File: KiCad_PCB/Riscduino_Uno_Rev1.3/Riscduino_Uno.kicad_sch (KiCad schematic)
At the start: 87 parts, among them J10 Conn_01x06_Pin, J11 USB_B_Micro, J12 Conn_01x08_Pin, J13 Conn_01x10_Pin, J2 Conn_01x03_Pin, J3 Conn_01x01, J4 Conn_02x04_Odd_Even, J5 ISP, J6 Conn_01x01, J7 Conn_01x01, J8 Conn_01x01, J9 Conn_01x08_Pin, SW1 4Pin Round Button SPST Straig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, U2 W25Q32JVSS, U3 23LC1024-I/P, U4 W25Q32JVSS, U5 Riscduino, U6 LM1117MP-3.3, U7 LM1117S-ADJ, U8 CH340C, X1 ASE-10.000MHZ-LC-T

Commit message: Update
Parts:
- added R19, R25: 0E, Riscduino:R_0603_1608Metric_Pad0.98x0.95mm_HandSolder, symbol Device:R
- D1: renamed from D2; footprint Riscduino:LED_0805_2012Metric_Pad1.15x1.40mm_HandSolder -> Riscduino.Library:LED_0805_2012Metric_Pad1.15x1.40mm_HandSolder
- D2: renamed from D3; footprint Riscduino:LED_0805_2012Metric_Pad1.15x1.40mm_HandSolder -> Riscduino.Library:LED_0805_2012Metric_Pad1.15x1.40mm_HandSolder
- D3: renamed from D1; footprint Riscduino:LED_0805_2012Metric_Pad1.15x1.40mm_HandSolder -> Riscduino.Library:LED_0805_2012Metric_Pad1.15x1.40mm_HandSolder
- D4, D5: footprint Riscduino:LED_0805_2012Metric_Pad1.15x1.40mm_HandSolder -> Riscduino.Library:LED_0805_2012Metric_Pad1.15x1.40mm_HandSolder
- X1: footprint Riscduino:Crystal_SMD_Abracon_ABM8G-4Pin_3.2x2.5mm -> Riscduino.Library:Crystal_SMD_Abracon_ABM8G-4Pin_3.2x2.5mm
- renumbered C6 to C10, C8 to C11, C14 to C12, C16 to C13, C19 to C14, C17 to C16, C18 to C17, C22 to C18, C21 to C19, C23 to C20, C24 to C21, C25 to C22, C10 to C23, C12 to C24, C20 to C25, C7 to C5, C9 to C6, C11 to C7, C13 to C8, C5 to C9, J5 to J1, J13 to J10, J2 to J11, J7 to J12, J10 to J2, J9 to J3, J6 to J4, J3 to J5, J4 to J6, J8 to J7, J11 to J8, J12 to J9, JP2 to JP1, JP1 to JP2, R2 to R1, R12 to R10, R5 to R11, R32 to R12, R14 to R13, R19 to R14, R23 to R15, R20 to R16, R21 to R17, R22 to R18, R4 to R2, R25 to R20, R27 to R21, R29 to R22, R28 to R23, R33 to R24, R15 to R26, R16 to R27, R24 to R28, R26 to R29, R6 to R3, R7 to R4, R3 to R5, R9 to R6, R8 to R7, R13 to R8, R11 to R9, U4 to U1, U3 to U2, U5 to U3, U6 to U4, U8 to U5, U7 to U6, U2 to U7
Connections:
- net ardunio_d0: now also R19.2; no longer U5.2 (TXD)
- net ardunio_d1: now also R25.2; no longer U5.3 (RXD)
- net mprj_io_12: no longer J10.8 (Pin_8)
- net mprj_io_30: now also J10.8 (Pin_8)
- new net: R19.1, U5.2 (TXD)
- new net: R25.1, U5.3 (RXD)

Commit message: Power Supervisory Circuit
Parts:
- added C28: 0.1uf, Riscduino.Library:C_0603_1608Metric_Pad1.08x0.95mm_HandSolder, symbol Device:C
- added U8: APX811, Package_TO_SOT_SMD:SOT-143_Handsoldering, symbol Power_Supervisor:MIC811TUY
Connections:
- net +3.3V: now also C28.1, U8.4 (VCC)
- net GND: now also C28.2, U8.1 (GND)
- net ~{RST}: now also U8.2 (~{RESET}); no longer C3.1, R1.2, R12.2, SW1.2
- new net ~{MR}: C3.1, R1.2, R12.2, SW1.2, U8.3 (~{MR})
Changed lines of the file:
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@@
   (junction (at 328.93 37.084) (diameter 0) (color 0 0 0 0)
   )
+  (junction (at 361.95 247.65) (diameter 0) (color 0 0 0 0)
+  )
   (junction (at 80.01 206.248) (diameter 0) (color 0 0 0 0)
   )
@@
   (junction (at 328.168 196.342) (diameter 0) (color 0 0 0 0)
   )
+  (junction (at 326.39 262.89) (diameter 0) (color 0 0 0 0)
+  )
   (junction (at 330.708 173.228) (diameter 0) (color 0 0 0 0)
   )
@@
     (stroke (width 0) (type default))
   )
-  (wire (pts (xy 323.85 262.89) (xy 332.994 262.89))
+  (wire (pts (xy 323.85 262.89) (xy 326.39 262.89))
     (stroke (width 0) (type default))
   )
@@
     (stroke (width 0) (type default))
   )
+  (wire (pts (xy 353.06 247.65) (xy 361.95 247.65))
+    (stroke (width 0) (type default))
+  )
   (wire (pts (xy 106.68 50.292) (xy 106.68 53.34))
     (stroke (width 0) (type default))
@@
     (stroke (width 0) (type default))
   )
+  (wire (pts (xy 353.06 270.51) (xy 353.06 273.05))
+    (stroke (width 0) (type default))
+  )
   (wire (pts (xy 127 29.972) (xy 153.416 29.972))
     (stroke (width 0) (type default))
@@
     (stroke (width 0) (type default))
   )
-  (wire (pts (xy 332.994 262.89) (xy 342.138 262.89))
-    (stroke (width 0) (type default))
-  )
   (wire (pts (xy 395.224 51.562) (xy 404.114 51.562))
     (stroke (width 0) (type default))
@@
     (stroke (width 0) (type default))
   )
+  (wire (pts (xy 326.39 267.97) (xy 326.39 262.89))
+    (stroke (width 0) (type default))
+  )
   (wire (pts (xy 315.468 134.62) (xy 337.566 134.62))
     (stroke (width 0) (type default))
@@
     (stroke (width 0) (type default))
   )
+  (wire (pts (xy 363.22 262.89) (xy 373.38 262.89))
+    (stroke (width 0) (type default))
+  )
   (wire (pts (xy 328.93 51.054) (xy 328.93 60.198))
     (stroke (width 0) (type default))
@@
     (stroke (width 0) (type default))
   )
+  (wire (pts (xy 332.994 262.89) (xy 342.9 262.89))
+    (stroke (width 0) (type default))
+  )
   (wire (pts (xy 116.84 49.53) (xy 116.84 53.34))
     (stroke (width 0) (type default))
@@
     (stroke (width 0) (type default))
   )
+  (wire (pts (xy 353.06 255.27) (xy 353.06 247.65))
+    (stroke (width 0) (type default))
+  )
   (wire (pts (xy 333.248 173.228) (xy 346.964 173.228))
     (stroke (width 0) (type default))
@@
     (stroke (width 0) (type default))
   )
+  (wire (pts (xy 369.57 247.65) (xy 369.57 248.92))
+    (stroke (width 0) (type default))
+  )
   (wire (pts (xy 331.47 37.084) (xy 331.47 43.434))
     (stroke (width 0) (type default))
@@
     (stroke (width 0) (type default))
   )
+  (wire (pts (xy 361.95 245.11) (xy 361.95 247.65))
+    (stroke (width 0) (type default))
+  )
   (wire (pts (xy 67.31 271.78) (xy 67.31 275.59))
     (stroke (width 0) (type default))
@@
     (stroke (width 0) (type default))
   )
+  (wire (pts (xy 322.58 267.97) (xy 326.39 267.97))
+    (stroke (width 0) (type default))
+  )
   (wire (pts (xy 304.8 364.49) (xy 317.5 364.49))
     (stroke (width 0) (type default))
@@
     (stroke (width 0) (type default))
   )
+  (wire (pts (xy 326.39 262.89) (xy 332.994 262.89))
+    (stroke (width 0) (type default))
+  )
   (wire (pts (xy 178.562 257.81) (xy 178.562 259.08))
     (stroke (width 0) (type default))
@@
     (stroke (width 0) (type default))
   )
+  (wire (pts (xy 361.95 247.65) (xy 369.57 247.65))
+    (stroke (width 0) (type default))
+  )
   (wire (pts (xy 80.01 83.82) (xy 86.36 83.82))
     (stroke (width 0) (type default))
@@
     )
   )
-  (global_label "~{RST}" (shape output) (at 342.138 262.89 0) (fields_autoplaced)
+  (global_label "~{RST}" (shape output) (at 373.38 262.89 0) (fields_autoplaced)
     (effects (font (size 1.27 1.27)) (justify left))
-    (property "Intersheetrefs" "${INTERSHEET_REFS}" (at 348.4909 262.89 0)
+    (property "Intersheetrefs" "${INTERSHEET_REFS}" (at 379.7329 262.89 0)
       (effects (font (size 1.27 1.27)) (justify left) hide)
     )
@@
     )
   )
-  (global_label "~{RST}" (shape output) (at 222.504 284.48 0) (fields_autoplaced)
+  (global_label "~{MR}" (shape output) (at 222.504 284.48 0) (fields_autoplaced)
     (effects (font (size 1.27 1.27)) (justify left))
-    (property "Intersheetrefs" "${INTERSHEET_REFS}" (at 228.8569 284.48 0)
+    (property "Intersheetrefs" "${INTERSHEET_REFS}" (at 228.2106 284.48 0)
       (effects (font (size 1.27 1.27)) (justify left) hide)
     )
@@
     )
   )
+  (global_label "~{MR}" (shape input) (at 322.58 267.97 180) (fields_autoplaced)
+    (effects (font (size 1.27 1.27)) (justify right))
+    (property "Intersheetrefs" "${INTERSHEET_REFS}" (at 316.8734 267.97 0)
+      (effects (font (size 1.27 1.27)) (justify right) hide)
+    )
+  )
   (global_label "CARAVEL_FLASH_IO1" (shape bidirectional) (at 314.452 198.882 180) (fields_autoplaced)
     (effects (font (size 1.27 1.27)) (justify right))
@@
     )
   )
+  (symbol (lib_id "power:GND") (at 353.06 273.05 0) (unit 1)
+    (in_bom yes) (on_board yes) (dnp no) (fields_autoplaced)
+    (property "Reference" "#PWR073" (at 353.06 279.4 0)
+      (effects (font (size 1.27 1.27)) hide)
+    )
+    (property "Value" "GND" (at 353.06 278.13 0)
+      (effects (font (size 1.27 1.27)))
+    )
+    (property "Footprint" "" (at 353.06 273.05 0)
+      (effects (font (size 1.27 1.27)) hide)
+    )
+    (property "Datasheet" "" (at 353.06 273.05 0)
+      (effects (font (size 1.27 1.27)) hide)
+    )
+    (pin "1")
+    (instances
+      (project "Riscduino_Uno"
+        (path "/3385a618-de98-459b-bc8d-0b8733b3fac9"
+          (reference "#PWR073") (unit 1)
+        )
+      )
+    )
+  )
   (symbol (lib_id "Device:LED") (at 491.744 318.008 0) (unit 1)
     (in_bom yes) (on_board yes) (dnp no)
@@
     )
   )
+  (symbol (lib_id "power:GND") (at 369.57 256.54 0) (unit 1)
+    (in_bom yes) (on_board yes) (dnp no) (fields_autoplaced)
+    (property "Reference" "#PWR087" (at 369.57 262.89 0)
+      (effects (font (size 1.27 1.27)) hide)
+    )
+    (property "Value" "GND" (at 369.57 261.62 0)
+      (effects (font (size 1.27 1.27)))
+    )
+    (property "Footprint" "" (at 369.57 256.54 0)
+      (effects (font (size 1.27 1.27)) hide)
+    )
+    (property "Datasheet" "" (at 369.57 256.54 0)
+      (effects (font (size 1.27 1.27)) hide)
+    )
+    (pin "1")
+    (instances
+      (project "Riscduino_Uno"
+        (path "/3385a618-de98-459b-bc8d-0b8733b3fac9"
+          (reference "#PWR087") (unit 1)
+        )
+      )
+    )
+  )
   (symbol (lib_id "Memory_Flash:W25Q32JVSS") (at 347.726 129.54 0) (unit 1)
     (in_bom yes) (on_board yes) (dnp no) (fields_autoplaced)
@@
     )
   )
+  (symbol (lib_id "Power_Supervisor:MIC811TUY") (at 353.06 262.89 0) (unit 1)
+    (in_bom yes) (on_board yes) (dnp no)
+    (property "Reference" "U8" (at 363.22 259.08 0)
+      (effects (font (size 1.27 1.27)))
+    )
+    (property "Value" "APX811" (at 360.68 255.27 0)
+      (effects (font (size 1.27 1.27)))
+    )
+    (property "Footprint" "Package_TO_SOT_SMD:SOT-143_Handsoldering" (at 355.6 270.51 0)
+      (effects (font (size 1.27 1.27)) (justify left) hide)
+    )
+    (property "Datasheet" "https://www.diodes.com/assets/Datasheets/APX811_812.pdf" (at 344.17 280.67 0)
+      (effects (font (size 1.27 1.27)) hide)
+    )
+    (pin "1")
+    (pin "2")
+    (pin "3")
+    (pin "4")
+    (instances
+      (project "Riscduino_Uno"
+        (path "/3385a618-de98-459b-bc8d-0b8733b3fac9"
+          (reference "U8") (unit 1)
+        )
+      )
+    )
+  )
   (symbol (lib_id "Device:R") (at 502.412 325.628 90) (unit 1)
     (in_bom yes) (on_board yes) (dnp no) (fields_autoplaced)
@@
     )
   )
+  (symbol (lib_id "Device:C") (at 369.57 252.73 0) (unit 1)
+    (in_bom yes) (on_board yes) (dnp no) (fields_autoplaced)
+    (property "Reference" "C28" (at 373.38 251.46 0)
+      (effects (font (size 1.27 1.27)) (justify left))
+    )
+    (property "Value" "0.1uf" (at 373.38 254 0)
+      (effects (font (size 1.27 1.27)) (justify left))
+    )
+    (property "Footprint" "Riscduino.Library:C_0603_1608Metric_Pad1.08x0.95mm_HandSolder" (at 370.5352 256.54 0)
+      (effects (font (size 1.27 1.27)) hide)
+    )
+    (property "Datasheet" "~" (at 369.57 252.73 0)
+      (effects (font (size 1.27 1.27)) hide)
+    )
+    (pin "1")
+    (pin "2")
+    (instances
+      (project "Riscduino_Uno"
+        (path "/3385a618-de98-459b-bc8d-0b8733b3fac9"
+          (reference "C28") (unit 1)
+        )
+      )
+    )
+  )
   (symbol (lib_id "power:+3.3V") (at 509.524 311.15 270) (unit 1)
     (in_bom yes) (on_board yes) (dnp no) (fields_autoplaced)
@@
         )
       )
+    )
+  )
+  (symbol (lib_id "power:+3.3V") (at 361.95 245.11 0) (unit 1)
+    (in_bom yes) (on_board yes) (dnp no)
+    (property "Reference" "#PWR088" (at 361.95 248.92 0)
+      (effects (font (size 1.27 1.27)) hide)
+    )
+    (property "Value" "+3.3V" (at 362.458 242.316 90)
+      (effects (font (size 1.27 1.27)) (justify left))
+    )
+    (property "Footprint" "" (at 361.95 245.11 0)
+      (effects (font (size 1.27 1.27)) hide)
+    )
+    (property "Datasheet" "" (at 361.95 245.11 0)
+      (effects (font (size 1.27 1.27)) hide)
+    )
+    (pin "1")
+    (instances
+      (project "Riscduino_Uno"
+        (path "/3385a618-de98-459b-bc8d-0b8733b3fac9"
+          (reference "#PWR088") (unit 1)
+        )
+      )

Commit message: update
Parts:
- U8: value APX811 -> APX811-29UG-7
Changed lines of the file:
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@@
   )
   (text_box "Reset Circuit"
-    (at 294.64 241.046 0) (size 124.46 50.8)
+    (at 294.64 234.95 0) (size 124.46 56.896)
     (stroke (width 0) (type default))
     (fill (type none))
@@
       (effects (font (size 1.27 1.27)))
     )
-    (property "Value" "APX811" (at 360.68 255.27 0)
+    (property "Value" "APX811-29UG-7" (at 365.76 270.51 0)
       (effects (font (size 1.27 1.27)))
     )

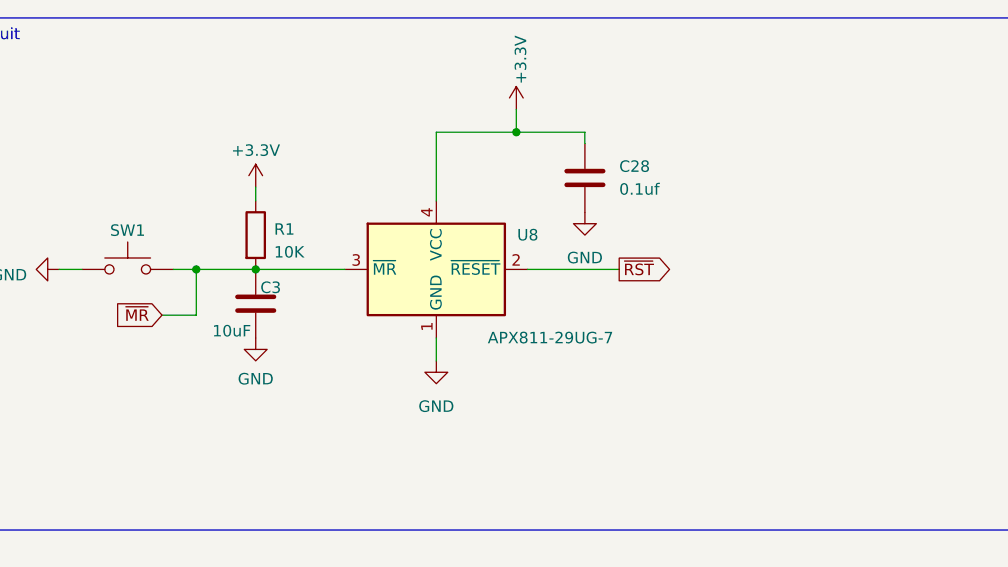
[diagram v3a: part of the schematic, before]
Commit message: 1.3 Uno Schematic update
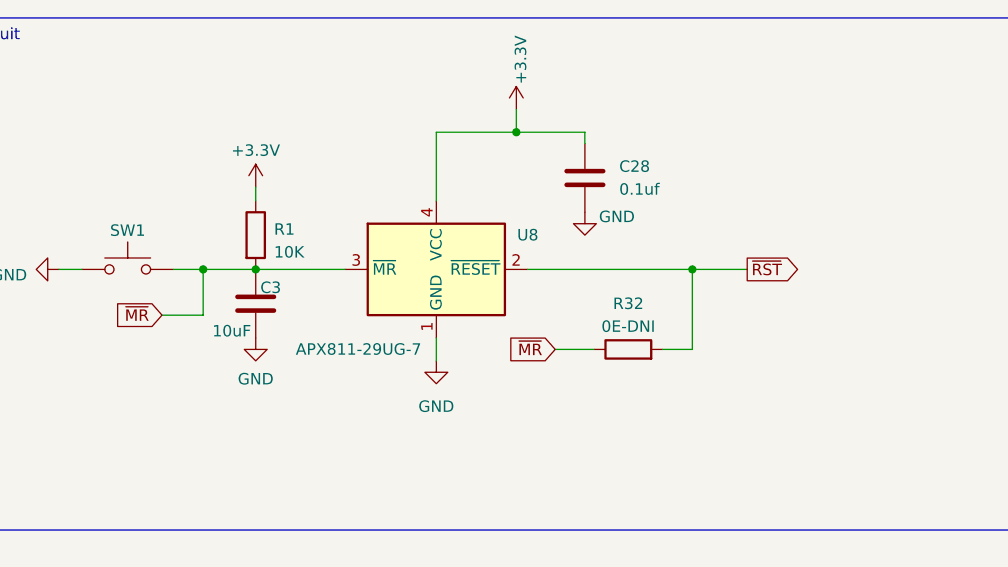
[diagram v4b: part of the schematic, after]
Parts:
- added R32: 0E-DNI, Riscduino:C_0603_1608Metric_Pad1.08x0.95mm_HandSolder, symbol Device:R
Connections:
- net ~{MR}: now also R32.1
- net ~{RST}: now also R32.2
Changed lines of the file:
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@@
   (junction (at 347.726 37.084) (diameter 0) (color 0 0 0 0)
   )
-  (junction (at 332.994 262.89) (diameter 0) (color 0 0 0 0)
-  )
   (junction (at 81.28 373.38) (diameter 0) (color 0 0 0 0)
   )
@@
   (junction (at 328.168 196.342) (diameter 0) (color 0 0 0 0)
   )
-  (junction (at 326.39 262.89) (diameter 0) (color 0 0 0 0)
-  )
   (junction (at 330.708 173.228) (diameter 0) (color 0 0 0 0)
   )
@@
   (junction (at 334.01 37.084) (diameter 0) (color 0 0 0 0)
   )
+  (junction (at 332.994 262.89) (diameter 0) (color 0 0 0 0)
+  )
   (junction (at 328.168 173.228) (diameter 0) (color 0 0 0 0)
   )
@@
   (junction (at 81.28 397.51) (diameter 0) (color 0 0 0 0)
   )
+  (junction (at 381.508 262.89) (diameter 0) (color 0 0 0 0)
+  )
   (junction (at 64.516 328.168) (diameter 0) (color 0 0 0 0)
   )
+  (junction (at 327.152 262.89) (diameter 0) (color 0 0 0 0)
+  )
   (junction (at 347.726 103.886) (diameter 0) (color 0 0 0 0)
   )
@@
     (stroke (width 0) (type default))
   )
+  (wire (pts (xy 327.152 267.97) (xy 327.152 262.89))
+    (stroke (width 0) (type default))
+  )
   (wire (pts (xy 508.762 318.77) (xy 508.762 318.008))
     (stroke (width 0) (type default))
@@
     (stroke (width 0) (type default))
   )
-  (wire (pts (xy 323.85 262.89) (xy 326.39 262.89))
-    (stroke (width 0) (type default))
-  )
   (wire (pts (xy 304.8 354.33) (xy 317.5 354.33))
     (stroke (width 0) (type default))
@@
     (stroke (width 0) (type default))
   )
+  (wire (pts (xy 323.85 262.89) (xy 327.152 262.89))
+    (stroke (width 0) (type default))
+  )
   (wire (pts (xy 73.66 311.912) (xy 72.136 311.912))
     (stroke (width 0) (type default))
@@
     (stroke (width 0) (type default))
   )
+  (wire (pts (xy 381.508 262.89) (xy 387.604 262.89))
+    (stroke (width 0) (type default))
+  )
+  (wire (pts (xy 378.206 271.78) (xy 381.508 271.78))
+    (stroke (width 0) (type default))
+  )
   (wire (pts (xy 486.664 332.994) (xy 488.442 332.994))
     (stroke (width 0) (type default))
@@
     (stroke (width 0) (type default))
   )
+  (wire (pts (xy 327.152 262.89) (xy 332.994 262.89))
+    (stroke (width 0) (type default))
+  )
   (wire (pts (xy 379.984 344.17) (xy 384.556 344.17))
     (stroke (width 0) (type default))
@@
     (stroke (width 0) (type default))
   )
+  (wire (pts (xy 363.22 262.89) (xy 381.508 262.89))
+    (stroke (width 0) (type default))
+  )
   (wire (pts (xy 311.15 262.89) (xy 313.69 262.89))
     (stroke (width 0) (type default))
@@
     (stroke (width 0) (type default))
   )
-  (wire (pts (xy 326.39 267.97) (xy 326.39 262.89))
-    (stroke (width 0) (type default))
-  )
   (wire (pts (xy 315.468 134.62) (xy 337.566 134.62))
     (stroke (width 0) (type default))
@@
     (stroke (width 0) (type default))
   )
-  (wire (pts (xy 363.22 262.89) (xy 373.38 262.89))
-    (stroke (width 0) (type default))
-  )
   (wire (pts (xy 328.93 51.054) (xy 328.93 60.198))
     (stroke (width 0) (type default))
@@
     (stroke (width 0) (type default))
   )
-  (wire (pts (xy 332.994 262.89) (xy 342.9 262.89))
-    (stroke (width 0) (type default))
-  )
   (wire (pts (xy 116.84 49.53) (xy 116.84 53.34))
     (stroke (width 0) (type default))
@@
     (stroke (width 0) (type default))
   )
+  (wire (pts (xy 366.268 271.78) (xy 370.586 271.78))
+    (stroke (width 0) (type default))
+  )
+  (wire (pts (xy 332.994 262.89) (xy 342.9 262.89))
+    (stroke (width 0) (type default))
+  )
   (wire (pts (xy 496.062 304.8) (xy 498.348 304.8))
     (stroke (width 0) (type default))
@@
     (stroke (width 0) (type default))
   )
+  (wire (pts (xy 322.58 267.97) (xy 327.152 267.97))
+    (stroke (width 0) (type default))
+  )
   (wire (pts (xy 376.428 376.428) (xy 383.032 376.428))
     (stroke (width 0) (type default))
@@
     (stroke (width 0) (type default))
   )
-  (wire (pts (xy 322.58 267.97) (xy 326.39 267.97))
-    (stroke (width 0) (type default))
-  )
   (wire (pts (xy 304.8 364.49) (xy 317.5 364.49))
     (stroke (width 0) (type default))
@@
     (stroke (width 0) (type default))
   )
-  (wire (pts (xy 326.39 262.89) (xy 332.994 262.89))
-    (stroke (width 0) (type default))
-  )
   (wire (pts (xy 178.562 257.81) (xy 178.562 259.08))
     (stroke (width 0) (type default))
@@
     (stroke (width 0) (type default))
   )
+  (wire (pts (xy 381.508 271.78) (xy 381.508 262.89))
+    (stroke (width 0) (type default))
+  )
   (wire (pts (xy 73.406 51.562) (xy 73.406 58.42))
     (stroke (width 0) (type default))
@@
     )
   )
+  (global_label "~{MR}" (shape input) (at 366.268 271.78 180) (fields_autoplaced)
+    (effects (font (size 1.27 1.27)) (justify right))
+    (property "Intersheetrefs" "${INTERSHEET_REFS}" (at 360.5614 271.78 0)
+      (effects (font (size 1.27 1.27)) (justify right) hide)
+    )
+  )
   (global_label "mprj_io_25" (shape bidirectional) (at 384.81 351.79 0) (fields_autoplaced)
     (effects (font (size 1.27 1.27)) (justify left))
@@
     )
   )
-  (global_label "~{RST}" (shape output) (at 373.38 262.89 0) (fields_autoplaced)
+  (global_label "~{RST}" (shape output) (at 387.604 262.89 0) (fields_autoplaced)
     (effects (font (size 1.27 1.27)) (justify left))
-    (property "Intersheetrefs" "${INTERSHEET_REFS}" (at 379.7329 262.89 0)
+    (property "Intersheetrefs" "${INTERSHEET_REFS}" (at 393.9569 262.89 0)
       (effects (font (size 1.27 1.27)) (justify left) hide)
     )
@@
   )
   (symbol (lib_id "power:GND") (at 369.57 256.54 0) (unit 1)
-    (in_bom yes) (on_board yes) (dnp no) (fields_autoplaced)
+    (in_bom yes) (on_board yes) (dnp no)
     (property "Reference" "#PWR087" (at 369.57 262.89 0)
       (effects (font (size 1.27 1.27)) hide)
     )
-    (property "Value" "GND" (at 369.57 261.62 0)
+    (property "Value" "GND" (at 373.126 257.048 0)
       (effects (font (size 1.27 1.27)))
     )
@@
     )
   )
+  (symbol (lib_id "Device:R") (at 374.396 271.78 90) (unit 1)
+    (in_bom yes) (on_board yes) (dnp no) (fields_autoplaced)
+    (property "Reference" "R32" (at 374.396 266.7 90)
+      (effects (font (size 1.27 1.27)))
+    )
+    (property "Value" "0E-DNI" (at 374.396 269.24 90)
+      (effects (font (size 1.27 1.27)))
+    )
+    (property "Footprint" "Riscduino:C_0603_1608Metric_Pad1.08x0.95mm_HandSolder" (at 374.396 273.558 90)
+      (effects (font (size 1.27 1.27)) hide)
+    )
+    (property "Datasheet" "~" (at 374.396 271.78 0)
+      (effects (font (size 1.27 1.27)) hide)
+    )
+    (pin "1")
+    (pin "2")
+    (instances
+      (project "Riscduino_Uno"
+        (path "/3385a618-de98-459b-bc8d-0b8733b3fac9"
+          (reference "R32") (unit 1)
+        )
+      )
+    )
+  )
   (symbol (lib_id "power:GND") (at 332.994 270.51 0) (unit 1)
     (in_bom yes) (on_board yes) (dnp no) (fields_autoplaced)
@@
       (effects (font (size 1.27 1.27)))
     )
-    (property "Value" "APX811-29UG-7" (at 365.76 270.51 0)
+    (property "Value" "APX811-29UG-7" (at 344.424 271.78 0)
       (effects (font (size 1.27 1.27)))
     )

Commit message: Riscduino Uno 1.3
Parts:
- renumbered C9 to C10, C10 to C11, C3 to C15, C15 to C16, C16 to C17, C17 to C18, C18 to C19, C19 to C20, C20 to C21, C21 to C22, C22 to C23, C23 to C24, C24 to C25, C25 to C26, C26 to C27, C27 to C28, C28 to C3, C11 to C5, C5 to C8, C8 to C9, J2 to J1, J1 to J2, R2 to R1, R11 to R10, R32 to R11, R1 to R13, R13 to R15, R17 to R16, R16 to R17, R15 to R18, R18 to R19, R4 to R2, R19 to R20, R20 to R21, R23 to R22, R22 to R23, R21 to R24, R24 to R25, R25 to R26, R26 to R27, R27 to R28, R28 to R29, R29 to R32, R5 to R4, R6 to R5, R7 to R6, R8 to R7, R9 to R8, R10 to R9, U8 to U1, U1 to U2, U2 to U3, U3 to U4, U4 to U5, U5 to U6, U6 to U7, U7 to U8
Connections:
- net ardunio_d11: now also U4.58 (mprj_io[20]); no longer U4.57 (mprj_io[19])
- net ardunio_d12: now also U4.57 (mprj_io[19]); no longer U4.58 (mprj_io[20])
